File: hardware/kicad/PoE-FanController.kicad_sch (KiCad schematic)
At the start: 31 parts, among them J2 FAN1, J3 FAN2, J4 FAN3, J5 FAN4, J6 Molex_KK254_3pin, J8 Waveshare_ESP32P4POEETH, U1 LM2587-12

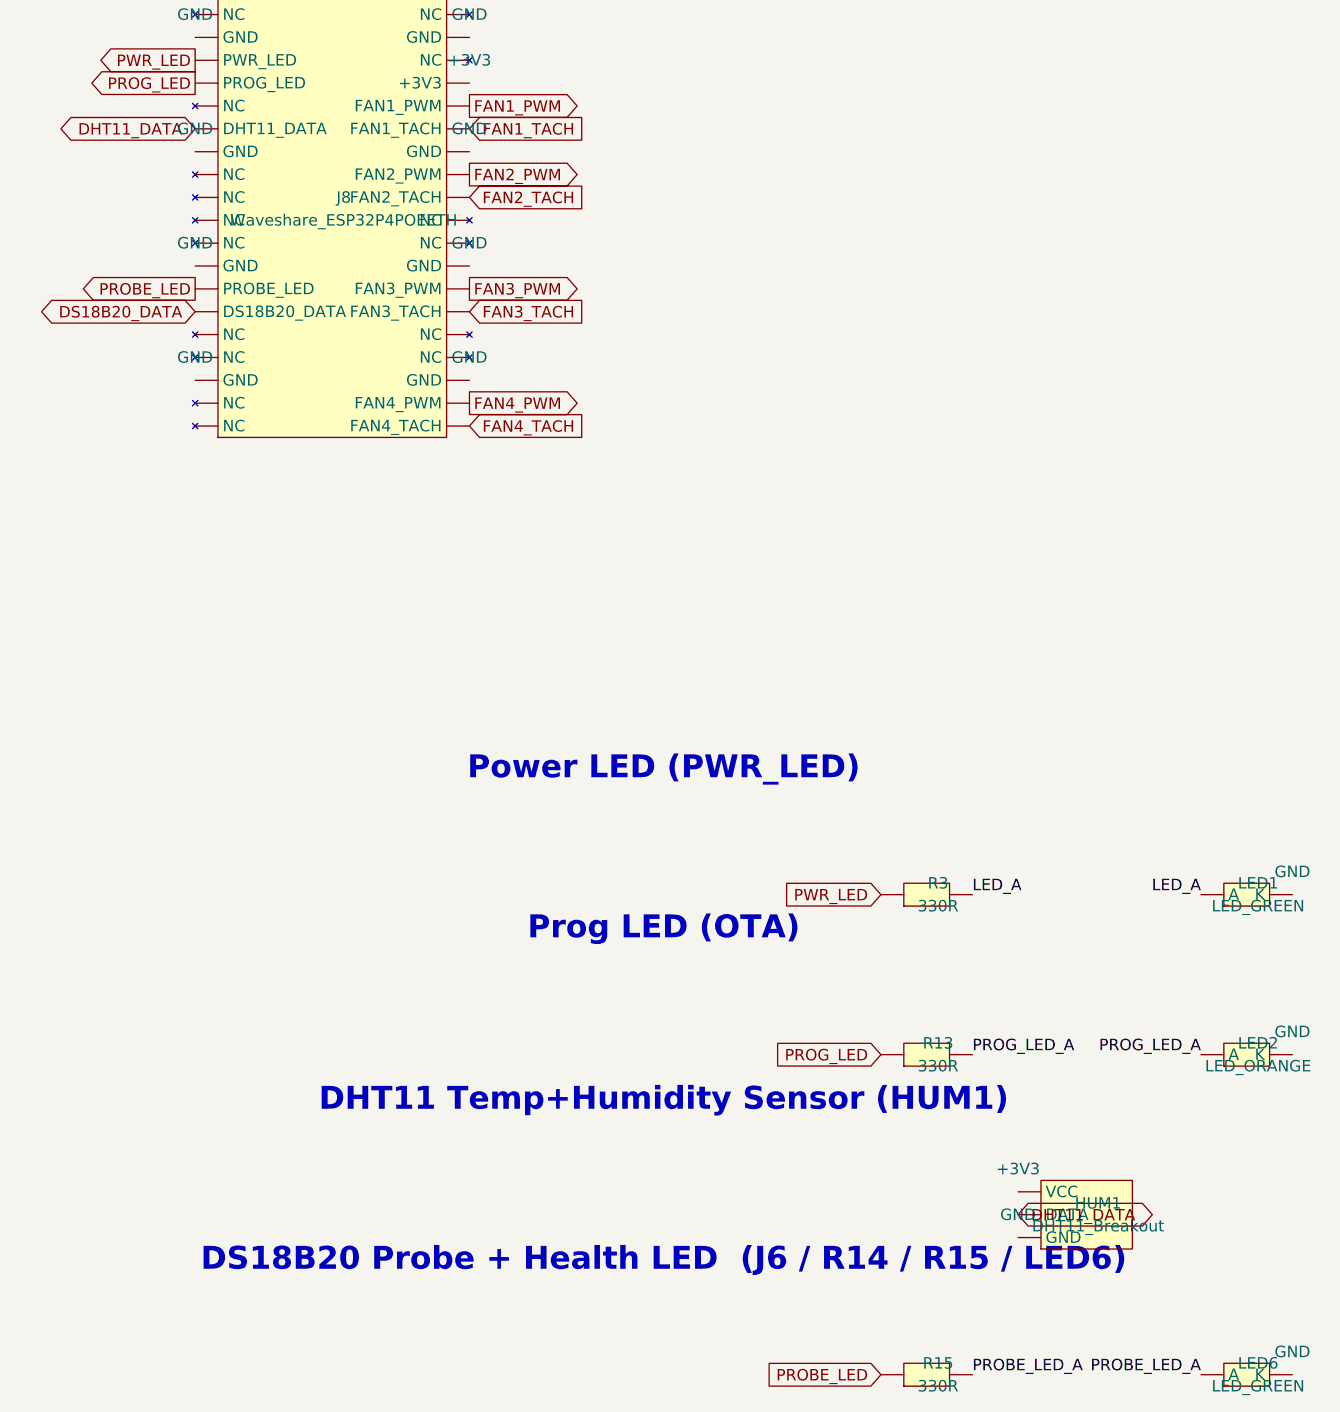
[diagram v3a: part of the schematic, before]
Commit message: hw(sch/pcb): 5-task overhaul — positions, pin swap, DHT11, traces
Task 1 — Record user-verified PCB component positions in fix_placement.py:
  User manually placed all components; coordinates read from saved PCB and
  committed to fix_placement.py as canonical reference. Key changes from
  previous script positions: J2-J5 rotated -90deg at x=73.12, fan LEDs/resistors
  repositioned, boost chain reorganised, LED circuits rotated.

Task 2 — PROBE_LED description updated:
  LED6 blinks only when DS18B20 probe data is actively received (firmware
  drives GPIO3 with pulse per 1-Wire read cycle). Comment added to schematic.

Task 3 — Swap PWM and TACH pins for all 4 fans:
  FAN1: PWM=pin34(GPIO21), TACH=pin35(GPIO20)  [was reversed]
  FAN2: PWM=pin31(GPIO23), TACH=pin32(GPIO22)  [was reversed]
  FAN3: PWM=pin26(GPIO32), TACH=pin27(GPIO27)  [was reversed]
  FAN4: PWM=pin21(GPIO48), TACH=pin22(GPIO47)  [was reversed]
  All 28 PCB pad nets updated accordingly.

Task 4 — Deleted all 125 existing PCB traces (clean slate for re-routing).

Task 5 — DHT11 changed from breakout module to direct 3-pin solder pads:
  Component renamed Custom:DHT11_Breakout → Custom:Conn_1x03 (same 3-pin
  PinHeader footprint). Solder DHT11 sensor legs directly to VCC/DATA/GND pads.

ERC: 0 errors

Co-authored-by: Copilot <223556219+Copilot@users.noreply.github.com>
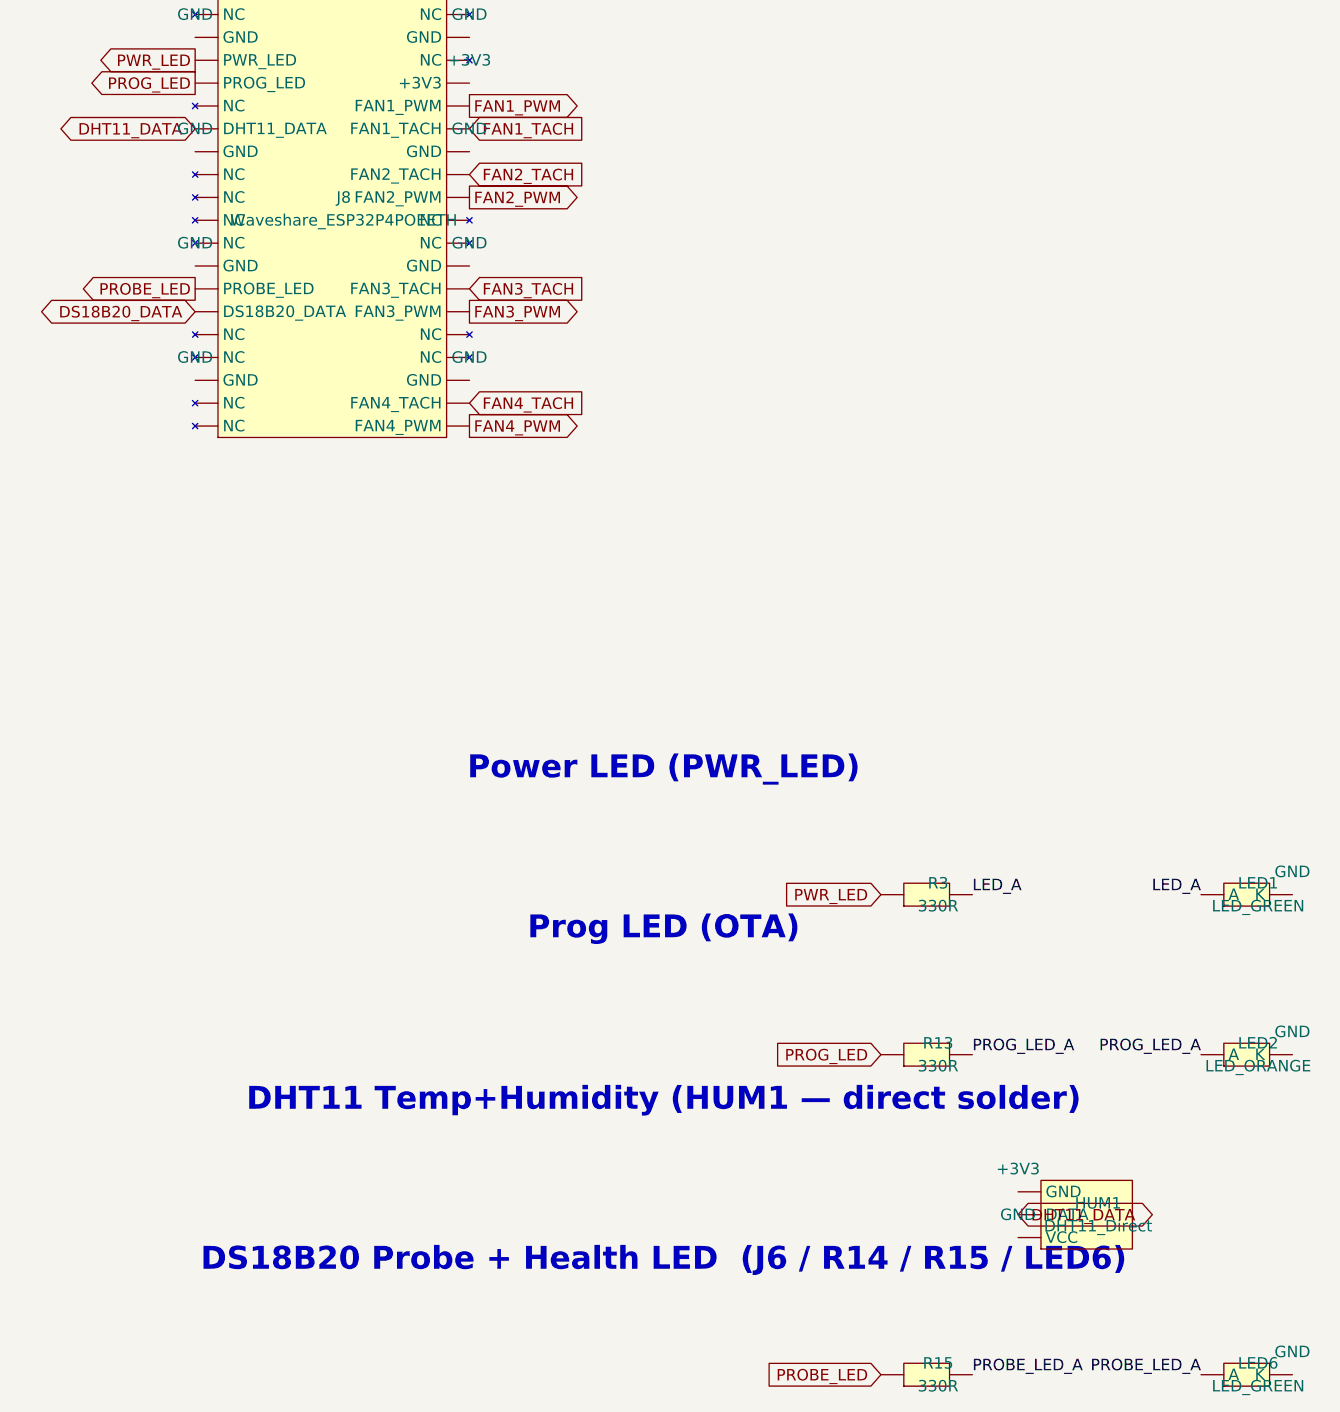
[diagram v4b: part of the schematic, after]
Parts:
- HUM1: value DHT11_Breakout -> DHT11_Direct; symbol Custom:DHT11_Breakout -> Custom:Conn_1x03
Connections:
- net FAN1_PWM: now also J8.34 (FAN1_PWM); no longer J8.35 (FAN1_PWM)
- net FAN1_TACH: now also J8.35 (FAN1_TACH); no longer J8.34 (FAN1_TACH)
- net FAN2_PWM: now also J8.31 (FAN2_PWM); no longer J8.32 (FAN2_PWM)
- net FAN2_TACH: now also J8.32 (FAN2_TACH); no longer J8.31 (FAN2_TACH)
- net FAN3_PWM: now also J8.26 (FAN3_PWM); no longer J8.27 (FAN3_PWM)
- net FAN3_TACH: now also J8.27 (FAN3_TACH); no longer J8.26 (FAN3_TACH)
- net FAN4_PWM: now also J8.21 (FAN4_PWM); no longer J8.22 (FAN4_PWM)
- net FAN4_TACH: now also J8.22 (FAN4_TACH); no longer J8.21 (FAN4_TACH)
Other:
- note added: "DHT11 Temp+Humidity (HUM1 — direct solder)"
- note removed: "DHT11 Temp+Humidity Sensor (HUM1)"
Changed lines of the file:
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@@
     (instances (project "PoE-FanController" (path "/" (reference "#PWR027") (unit 1))))
   )
-  (text "DHT11 Temp+Humidity Sensor (HUM1)" (at 128.2700 251.4600 0)
+  (text "DHT11 Temp+Humidity (HUM1 — direct solder)" (at 128.2700 251.4600 0)
     (effects (font (color 0 0 255 1) (bold yes) (size 2.54 2.54)))
 )
-  (symbol (lib_id "Custom:DHT11_Breakout") (at 175.2600 264.1600 0)
+  (symbol (lib_id "Custom:Conn_1x03") (at 175.2600 264.1600 0)
     (unit 1) (exclude_from_sim no) (in_bom yes) (on_board yes) (dnp no)
     (property "Reference" "HUM1"
       (at 176.5300 262.8900 0)
       (effects (font (size 1.27 1.27))))
-    (property "Value" "DHT11_Breakout"
+    (property "Value" "DHT11_Direct"
       (at 176.5300 265.4300 0)
       (effects (font (size 1.27 1.27))))
@@
     (pin "37")
     (pin "36")
+    (pin "34")
     (pin "35")
-    (pin "34")
     (pin "33")
     (pin "32")
@@
     (instances (project "PoE-FanController" (path "/" (reference "#PWR041") (unit 1))))
   )
+  (global_label "FAN2_TACH"
+    (shape input)
+    (at 106.6800 148.5900 0)
+    (fields_autoplaced yes)
+    (effects (font (size 1.27 1.27)) (justify left))
+    (property "Intersheetrefs" "${INTERSHEET_REFS}"
+      (at 114.3000 148.5900 0)
+      (effects (font (size 1.27 1.27)) (justify left) (hide yes)))
+  )
   (global_label "FAN2_PWM"
     (shape output)
-    (at 106.6800 148.5900 0)
-    (fields_autoplaced yes)
-    (effects (font (size 1.27 1.27)) (justify left))
-    (property "Intersheetrefs" "${INTERSHEET_REFS}"
-      (at 114.3000 148.5900 0)
-      (effects (font (size 1.27 1.27)) (justify left) (hide yes)))
-  )
-  (global_label "FAN2_TACH"
+    (at 106.6800 151.1300 0)
+    (fields_autoplaced yes)
+    (effects (font (size 1.27 1.27)) (justify left))
+    (property "Intersheetrefs" "${INTERSHEET_REFS}"
+      (at 114.3000 151.1300 0)
+      (effects (font (size 1.27 1.27)) (justify left) (hide yes)))
+  )
+  (global_label "FAN3_TACH"
     (shape input)
-    (at 106.6800 151.1300 0)
-    (fields_autoplaced yes)
-    (effects (font (size 1.27 1.27)) (justify left))
-    (property "Intersheetrefs" "${INTERSHEET_REFS}"
-      (at 114.3000 151.1300 0)
+    (at 106.6800 161.2900 0)
+    (fields_autoplaced yes)
+    (effects (font (size 1.27 1.27)) (justify left))
+    (property "Intersheetrefs" "${INTERSHEET_REFS}"
+      (at 114.3000 161.2900 0)
       (effects (font (size 1.27 1.27)) (justify left) (hide yes)))
   )
   (global_label "FAN3_PWM"
     (shape output)
-    (at 106.6800 161.2900 0)
-    (fields_autoplaced yes)
-    (effects (font (size 1.27 1.27)) (justify left))
-    (property "Intersheetrefs" "${INTERSHEET_REFS}"
-      (at 114.3000 161.2900 0)
-      (effects (font (size 1.27 1.27)) (justify left) (hide yes)))
-  )
-  (global_label "FAN3_TACH"
-    (shape input)
     (at 106.6800 163.8300 0)
     (fields_autoplaced yes)
@@
     (instances (project "PoE-FanController" (path "/" (reference "#PWR042") (unit 1))))
   )
+  (global_label "FAN4_TACH"
+    (shape input)
+    (at 106.6800 173.9900 0)
+    (fields_autoplaced yes)
+    (effects (font (size 1.27 1.27)) (justify left))
+    (property "Intersheetrefs" "${INTERSHEET_REFS}"
+      (at 114.3000 173.9900 0)
+      (effects (font (size 1.27 1.27)) (justify left) (hide yes)))
+  )
   (global_label "FAN4_PWM"
     (shape output)
-    (at 106.6800 173.9900 0)
-    (fields_autoplaced yes)
-    (effects (font (size 1.27 1.27)) (justify left))
-    (property "Intersheetrefs" "${INTERSHEET_REFS}"
-      (at 114.3000 173.9900 0)
-      (effects (font (size 1.27 1.27)) (justify left) (hide yes)))
-  )
-  (global_label "FAN4_TACH"
-    (shape input)
     (at 106.6800 176.5300 0)
     (fields_autoplaced yes)

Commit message: fix(sch/pcb): remap FAN3 pins + single-layer board
Schematic fixes (components.py regenerated):
1. PROBE_LED: removed from PIN21 — now only on PIN7 (GPIO3)
2. FAN3_TACH: PIN27 → PIN25 (GPIO33); adjacent pair with FAN3_PWM
3. FAN3_PWM:  PIN26 → PIN24 (GPIO46)
   - Pins 26 & 27 are now NC
   - All fan pairs now on adjacent pins:
     FAN1: TACH=35 / PWM=34
     FAN2: TACH=32 / PWM=31
     FAN3: TACH=25 / PWM=24
     FAN4: TACH=22 / PWM=21
   - R5→PIN35, R6→PIN32, R7→PIN25, R9→PIN34,
     R10→PIN31, R11→PIN24, R12→PIN21 (all correct)
   ERC: 0 errors, 74 pre-existing lib_symbol_mismatch warnings

PCB change:
9. Removed B.Cu copper layer — board is now single-layer (F.Cu only).
   Crossing routes will be handled with jumper wires.

Co-authored-by: Copilot <223556219+Copilot@users.noreply.github.com>
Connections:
- net FAN3_PWM: now also J8.24 (FAN3_PWM); no longer J8.26 (FAN3_PWM)
- net FAN3_TACH: now also J8.25 (FAN3_TACH); no longer J8.27 (FAN3_TACH)
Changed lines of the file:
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@@
     (pin "29")
     (pin "28")
+    (pin "25")
+    (pin "24")
     (pin "27")
     (pin "26")
-    (pin "25")
-    (pin "24")
     (pin "23")
     (pin "22")

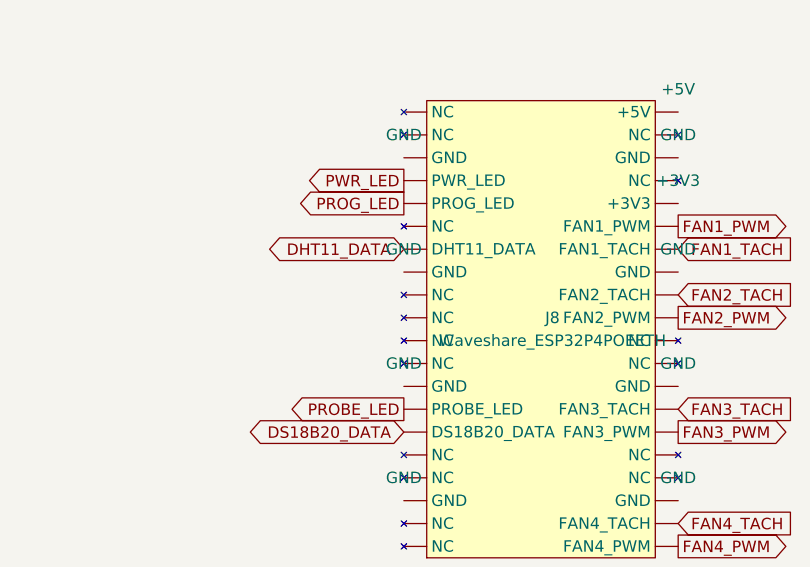
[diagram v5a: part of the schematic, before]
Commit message: fix(sch/pcb): move DHT11_DATA from PIN 14 to PIN 11
Schematic (components.py):
  - Pin 14: DHT11_DATA -> NC (was GPIO15)
  - Pin 11: NC -> DHT11_DATA (GPIO6)

PCB (pad nets synced):
  - J8 pad 14: DHT11_DATA -> (NC)
  - J8 pad 11: (NC) -> DHT11_DATA

Co-authored-by: Copilot <223556219+Copilot@users.noreply.github.com>
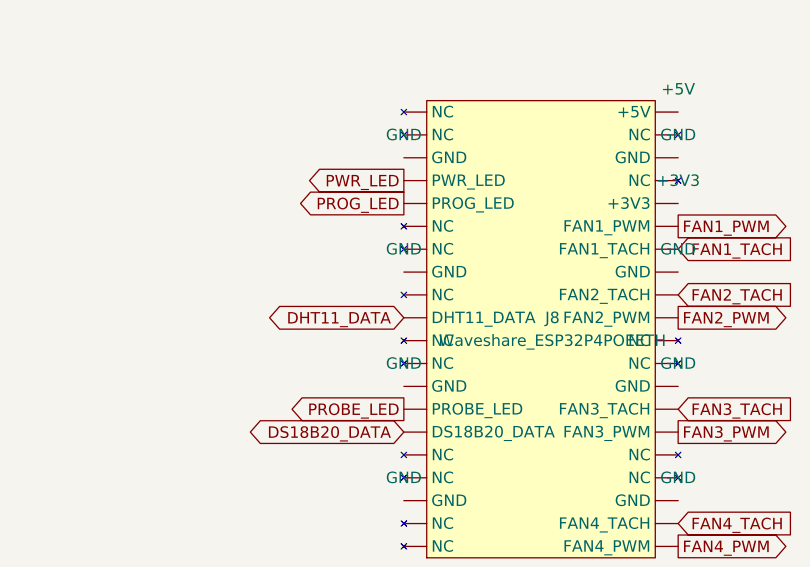
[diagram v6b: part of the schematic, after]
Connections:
- net DHT11_DATA: now also J8.11 (DHT11_DATA); no longer J8.14 (DHT11_DATA)
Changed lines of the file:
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@@
   (global_label "DHT11_DATA"
     (shape bidirectional)
-    (at 76.2000 143.5100 180)
+    (at 76.2000 151.1300 180)
     (fields_autoplaced yes)
     (effects (font (size 1.27 1.27)) (justify right))
     (property "Intersheetrefs" "${INTERSHEET_REFS}"
-      (at 83.8200 143.5100 180)
+      (at 83.8200 151.1300 180)
       (effects (font (size 1.27 1.27)) (justify right) (hide yes)))
   )

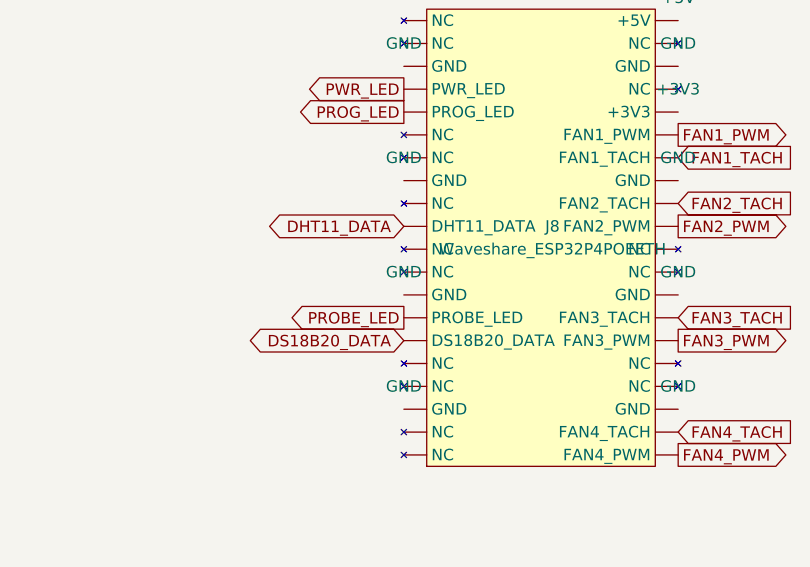
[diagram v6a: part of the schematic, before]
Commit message: fix(sch/pcb): move PROBE_LED (R15) from PIN 7 to PIN 10
Schematic (components.py):
  - Pin 7:  PROBE_LED -> NC (was GPIO3)
  - Pin 10: NC -> PROBE_LED (GPIO5)

PCB (pad nets synced):
  - J8 pad 7:  PROBE_LED -> (NC)
  - J8 pad 10: (NC) -> PROBE_LED

Co-authored-by: Copilot <223556219+Copilot@users.noreply.github.com>
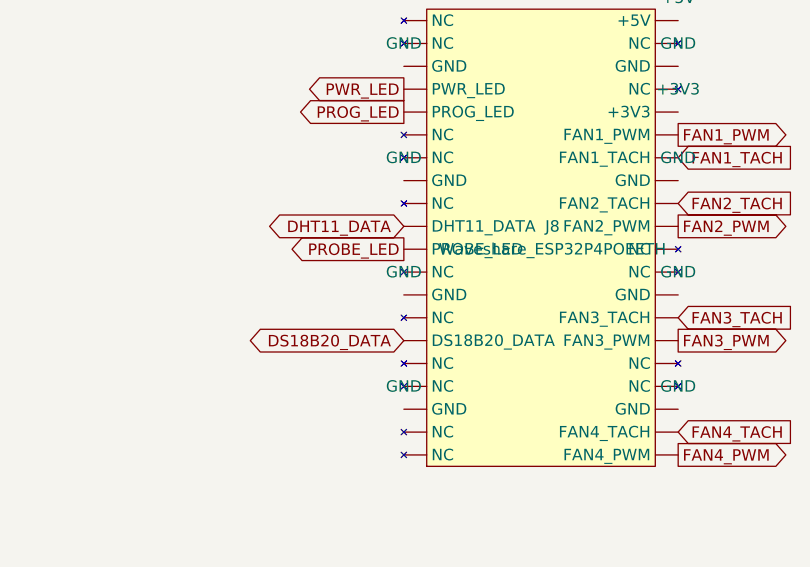
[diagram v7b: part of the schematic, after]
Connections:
- net PROBE_LED: now also J8.10 (PROBE_LED); no longer J8.7 (PROBE_LED)
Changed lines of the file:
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@@
   (global_label "PROBE_LED"
     (shape output)
-    (at 76.2000 161.2900 180)
+    (at 76.2000 153.6700 180)
     (fields_autoplaced yes)
     (effects (font (size 1.27 1.27)) (justify right))
     (property "Intersheetrefs" "${INTERSHEET_REFS}"
-      (at 83.8200 161.2900 180)
+      (at 83.8200 153.6700 180)
       (effects (font (size 1.27 1.27)) (justify right) (hide yes)))
   )
